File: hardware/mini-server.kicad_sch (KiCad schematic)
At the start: 0 parts

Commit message: Made a new power schematic and a new DDR4 ram schematic
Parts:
- added U1: RK3562, Package_BGA:RK3562, symbol easyeda2kicad:RK3562
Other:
- added sheet DDR4_PHY (DDR4_PHY.kicad_sch)
- added sheet Power (power.kicad_sch)

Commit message: DDR4 schematic almost completed
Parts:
- removed U1: RK3562, Package_BGA:RK3562, symbol easyeda2kicad:RK3562
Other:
- added sheet RK3562_CORE (core.kicad_sch)
- sheet DDR4_PHY ports: added DDR4_ctrl, DDR4_data; removed none

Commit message: New SoC
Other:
- removed sheet DDR4_PHY
- removed sheet Power
- removed sheet RK3562_CORE
- added sheet DDR3 (DDR3.kicad_sch)
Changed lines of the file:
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@@
 	(generator_version "9.0")
 	(paper "A4")
-	(wire
-		(pts
-			(xy 187.96 106.68) (xy 198.12 106.68)
-		)
-		(stroke
-			(width 0)
-			(type default)
-			(color 0 255 255 1)
-		)
-	)
-	(wire
-		(pts
-			(xy 187.96 109.22) (xy 198.12 109.22)
-		)
-		(stroke
-			(width 0)
-			(type default)
-		)
-	)
 	(sheet
-		(at 198.12 86.36)
-		(size 63.5 44.45)
+		(at 193.04 83.185)
+		(size 46.99 27.305)
 		(exclude_from_sim no)
 		(in_bom yes)
@@
 			(color 0 0 0 0.0000)
 		)
-		(property "Sheetname" "DDR4_PHY"
-			(at 198.12 85.6484 0)
+		(property "Sheetname" "DDR3"
+			(at 193.04 82.4734 0)
 			(effects
 				(font
@@
 			)
 		)
-		(property "Sheetfile" "DDR4_PHY.kicad_sch"
-			(at 198.12 131.3946 0)
-			(effects
-				(font
-					(size 1.27 1.27)
-				)
-				(justify left top)
-			)
-		)
-		(pin "DDR4_data" input
-			(at 198.12 106.68 180)
-			(effects
-				(font
-					(size 1.27 1.27)
-				)
-				(justify left)
-			)
-		)
-		(pin "DDR4_ctrl" input
-			(at 198.12 109.22 180)
-			(effects
-				(font
-					(size 1.27 1.27)
-				)
-				(justify left)
-			)
-		)
-		(instances
-			(project "mini-server"
-				(path "/17ecef2a-4000-49de-93ef-dcbfcfdaa69f"
-					(page "3")
-				)
-			)
-		)
-	)
-	(sheet
-		(at 135.89 95.25)
-		(size 52.07 21.59)
-		(exclude_from_sim no)
-		(in_bom yes)
-		(on_board yes)
-		(dnp no)
-		(fields_autoplaced yes)
-		(stroke
-			(width 0.1524)
-			(type solid)
-		)
-		(fill
-			(color 0 0 0 0.0000)
-		)
-		(property "Sheetname" "RK3562_CORE"
-			(at 135.89 94.5384 0)
-			(effects
-				(font
-					(size 1.27 1.27)
-				)
-				(justify left bottom)
-			)
-		)
-		(property "Sheetfile" "core.kicad_sch"
-			(at 135.89 117.4246 0)
-			(effects
-				(font
-					(size 1.27 1.27)
-				)
-				(justify left top)
-			)
-		)
-		(pin "DDR4_data" input
-			(at 187.96 106.68 0)
-			(effects
-				(font
-					(size 1.27 1.27)
-				)
-				(justify right)
-			)
-		)
-		(pin "DDR4_ctrl" input
-			(at 187.96 109.22 0)
-			(effects
-				(font
-					(size 1.27 1.27)
-				)
-				(justify right)
-			)
-		)
-		(instances
-			(project "mini-server"
-				(path "/17ecef2a-4000-49de-93ef-dcbfcfdaa69f"
-					(page "2")
-				)
-			)
-		)
-	)
-	(sheet
-		(at 39.37 81.28)
-		(size 54.61 49.53)
-		(exclude_from_sim no)
-		(in_bom yes)
-		(on_board yes)
-		(dnp no)
-		(fields_autoplaced yes)
-		(stroke
-			(width 0.1524)
-			(type solid)
-		)
-		(fill
-			(color 0 0 0 0.0000)
-		)
-		(property "Sheetname" "Power"
-			(at 39.37 80.5684 0)
-			(effects
-				(font
-					(size 1.27 1.27)
-				)
-				(justify left bottom)
-			)
-		)
-		(property "Sheetfile" "power.kicad_sch"
-			(at 39.37 131.3946 0)
+		(property "Sheetfile" "DDR3.kicad_sch"
+			(at 193.04 111.0746 0)
 			(effects
 				(font
@@
 			(project "mini-server"
 				(path "/17ecef2a-4000-49de-93ef-dcbfcfdaa69f"
-					(page "4")
+					(page "2")
 				)
 			)

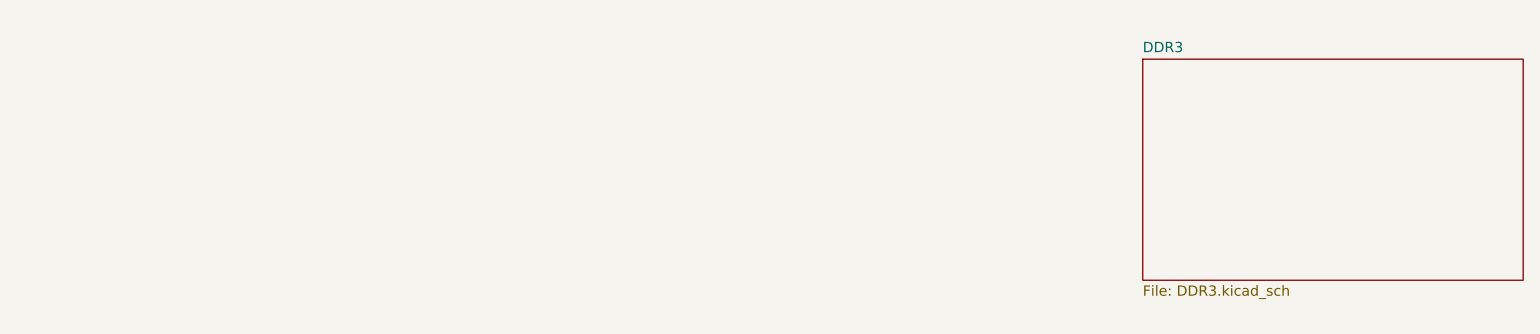
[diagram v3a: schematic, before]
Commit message: Address and Control signals of DDR3 ram routed
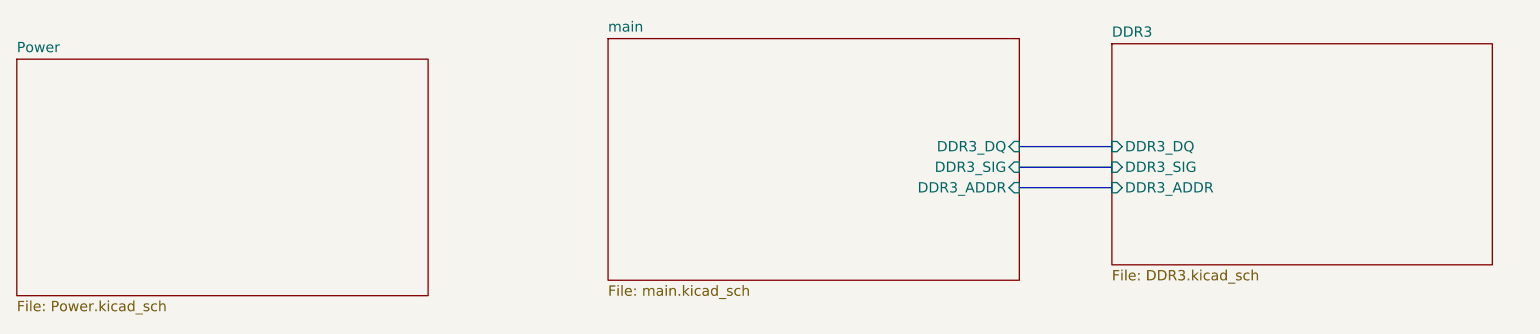
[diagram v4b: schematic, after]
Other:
- added sheet Power (Power.kicad_sch)
- added sheet main (main.kicad_sch)
- sheet DDR3 ports: added DDR3_ADDR, DDR3_DQ, DDR3_SIG; removed none
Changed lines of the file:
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@@
 	(generator_version "9.0")
 	(paper "A4")
+	(bus
+		(pts
+			(xy 177.8 99.06) (xy 189.23 99.06)
+		)
+		(stroke
+			(width 0)
+			(type default)
+		)
+	)
+	(bus
+		(pts
+			(xy 177.8 96.52) (xy 189.23 96.52)
+		)
+		(stroke
+			(width 0)
+			(type default)
+		)
+	)
+	(bus
+		(pts
+			(xy 177.8 93.98) (xy 189.23 93.98)
+		)
+		(stroke
+			(width 0)
+			(type default)
+		)
+	)
 	(sheet
-		(at 193.04 83.185)
+		(at 53.975 83.185)
+		(size 50.8 29.21)
+		(exclude_from_sim no)
+		(in_bom yes)
+		(on_board yes)
+		(dnp no)
+		(fields_autoplaced yes)
+		(stroke
+			(width 0.1524)
+			(type solid)
+		)
+		(fill
+			(color 0 0 0 0.0000)
+		)
+		(property "Sheetname" "Power"
+			(at 53.975 82.4734 0)
+			(effects
+				(font
+					(size 1.27 1.27)
+				)
+				(justify left bottom)
+			)
+		)
+		(property "Sheetfile" "Power.kicad_sch"
+			(at 53.975 112.9796 0)
+			(effects
+				(font
+					(size 1.27 1.27)
+				)
+				(justify left top)
+			)
+		)
+		(instances
+			(project "mini-server"
+				(path "/17ecef2a-4000-49de-93ef-dcbfcfdaa69f"
+					(page "4")
+				)
+			)
+		)
+	)
+	(sheet
+		(at 127 80.645)
+		(size 50.8 29.845)
+		(exclude_from_sim no)
+		(in_bom yes)
+		(on_board yes)
+		(dnp no)
+		(fields_autoplaced yes)
+		(stroke
+			(width 0.1524)
+			(type solid)
+		)
+		(fill
+			(color 0 0 0 0.0000)
+		)
+		(property "Sheetname" "main"
+			(at 127 79.9334 0)
+			(effects
+				(font
+					(size 1.27 1.27)
+				)
+				(justify left bottom)
+			)
+		)
+		(property "Sheetfile" "main.kicad_sch"
+			(at 127 111.0746 0)
+			(effects
+				(font
+					(size 1.27 1.27)
+				)
+				(justify left top)
+			)
+		)
+		(pin "DDR3_ADDR" input
+			(at 177.8 99.06 0)
+			(effects
+				(font
+					(size 1.27 1.27)
+				)
+				(justify right)
+			)
+		)
+		(pin "DDR3_DQ" input
+			(at 177.8 93.98 0)
+			(effects
+				(font
+					(size 1.27 1.27)
+				)
+				(justify right)
+			)
+		)
+		(pin "DDR3_SIG" input
+			(at 177.8 96.52 0)
+			(effects
+				(font
+					(size 1.27 1.27)
+				)
+				(justify right)
+			)
+		)
+		(instances
+			(project "mini-server"
+				(path "/17ecef2a-4000-49de-93ef-dcbfcfdaa69f"
+					(page "2")
+				)
+			)
+		)
+	)
+	(sheet
+		(at 189.23 81.28)
 		(size 46.99 27.305)
 		(exclude_from_sim no)
@@
 		)
 		(property "Sheetname" "DDR3"
-			(at 193.04 82.4734 0)
+			(at 189.23 80.5684 0)
 			(effects
 				(font
@@
 		)
 		(property "Sheetfile" "DDR3.kicad_sch"
-			(at 193.04 111.0746 0)
+			(at 189.23 109.1696 0)
 			(effects
 				(font
@@
 				)
 				(justify left top)
+			)
+		)
+		(pin "DDR3_DQ" input
+			(at 189.23 93.98 180)
+			(effects
+				(font
+					(size 1.27 1.27)
+				)
+				(justify left)
+			)
+		)
+		(pin "DDR3_SIG" input
+			(at 189.23 96.52 180)
+			(effects
+				(font
+					(size 1.27 1.27)
+				)
+				(justify left)
+			)
+		)
+		(pin "DDR3_ADDR" input
+			(at 189.23 99.06 180)
+			(effects
+				(font
+					(size 1.27 1.27)
+				)
+				(justify left)
 			)
 		)
@@
 			(project "mini-server"
 				(path "/17ecef2a-4000-49de-93ef-dcbfcfdaa69f"
-					(page "2")
-				)
-			)
+					(page "3")
+				)
+			)
